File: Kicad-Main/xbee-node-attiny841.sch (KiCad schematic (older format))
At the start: 42 parts, among them P10 CONN_1, P11 CONN_1, P12 CONN_1, P13 CONN_1, P14 CONN_1, P15 CONN_1, P16 CONN_1, P17 CONN_1, P18 CONN_1, P19 CONN_1, P2 XBee Adaptor, P20 CONN_1, P3 Debug Adaptor, P7 CONN_1, P8 CONN_1, P9 CONN_1, Q1 BSS84, Q2 MMBT3904, Q3 2N7002, U1 ATTINY841, U2 MAX952ESA, U3 TPS77033

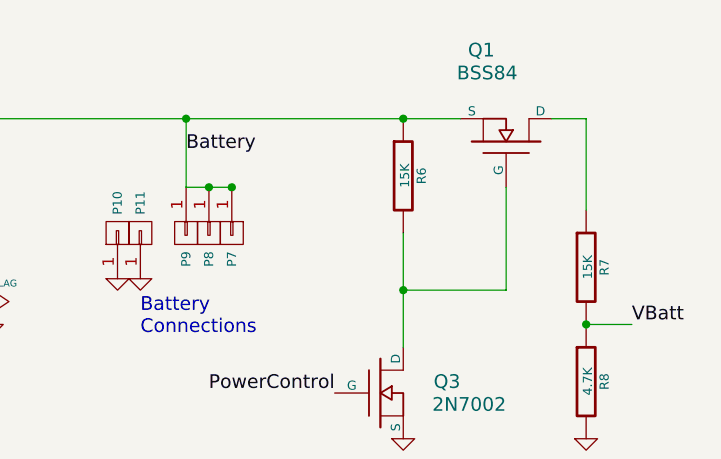
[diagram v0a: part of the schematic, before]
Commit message: Main board PCB: generation of extra gerber layers
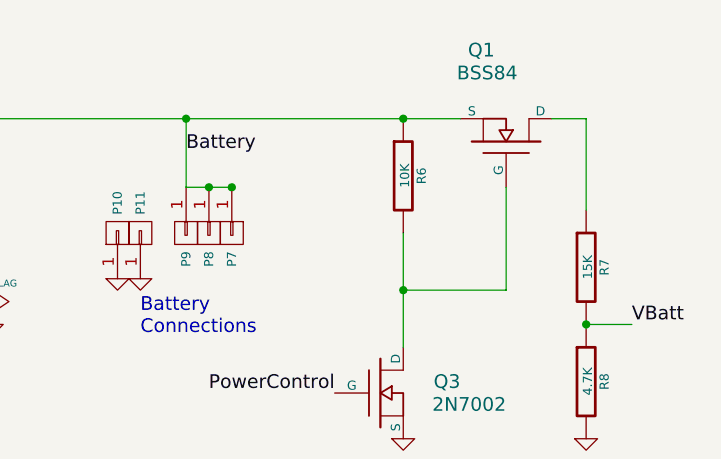
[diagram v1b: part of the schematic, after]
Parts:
- R6: value 15K -> 10K
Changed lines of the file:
@@
 P 9450 1650
 F 0 "R6" V 9530 1650 40  0000 C CNN
-F 1 "15K" V 9457 1651 40  0000 C CNN
+F 1 "10K" V 9457 1651 40  0000 C CNN
 F 2 "PhotoDiode:SM0603_Resistor" V 9380 1650 30  0001 C CNN
 F 3 "" H 9450 1650 30  0000 C CNN
